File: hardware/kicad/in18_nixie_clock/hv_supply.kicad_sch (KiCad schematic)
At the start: 2 parts

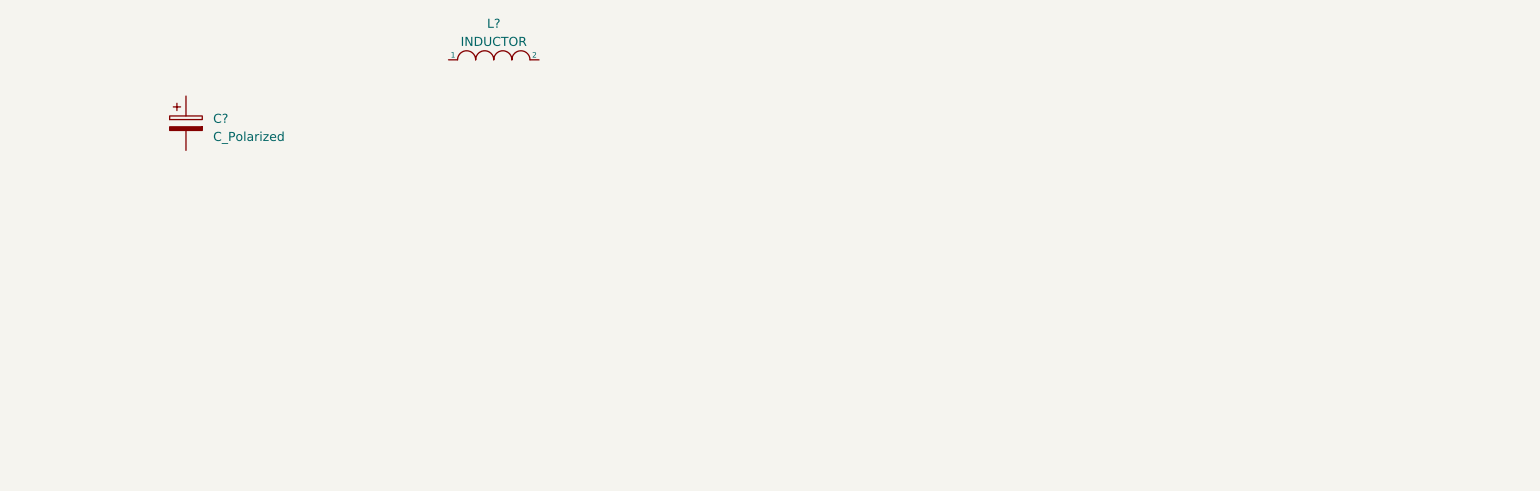
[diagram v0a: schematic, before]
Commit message: Delete backups. Add HV supply schematic
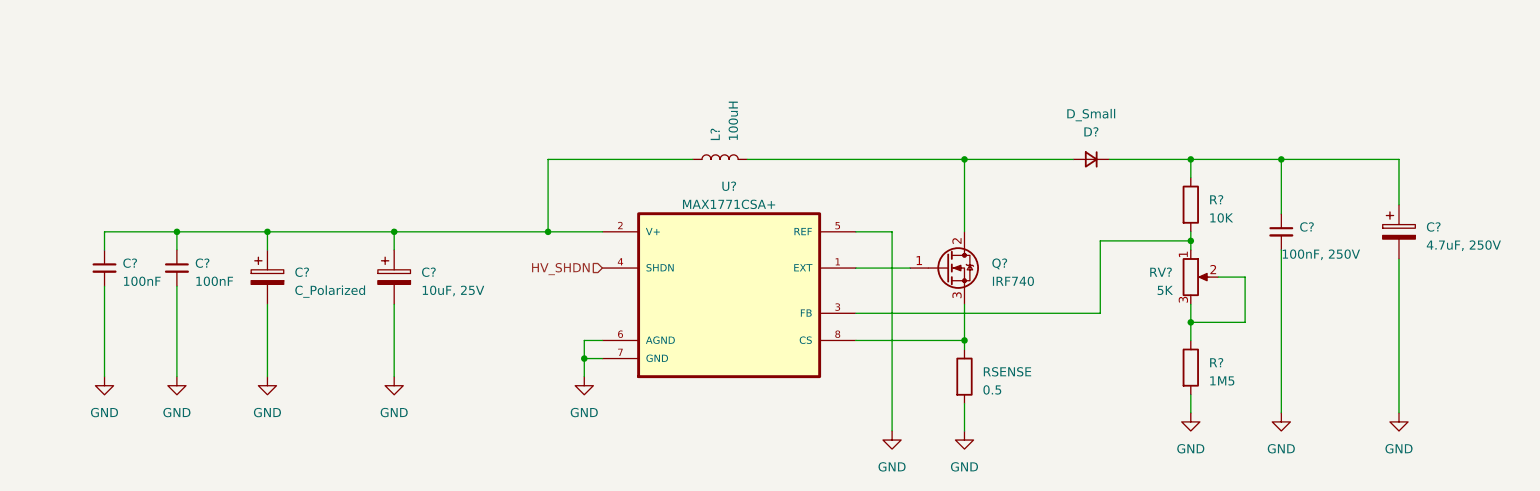
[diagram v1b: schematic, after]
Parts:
- removed L?: INDUCTOR, symbol pspice:INDUCTOR
- added C?: 4.7uF, 250V, symbol Device:C_Polarized
- added C?: 10uF, 25V, symbol Device:C_Polarized
- added C? (x2): 100nF, Capacitor_SMD:C_0805_2012Metric_Pad1.18x1.45mm_HandSolder, symbol Device:C_Small
- added C?: 100nF, 250V, Capacitor_SMD:C_0805_2012Metric_Pad1.18x1.45mm_HandSolder, symbol Device:C_Small
- added D?: D_Small, symbol Device:D_Small
- added L?: 100uH, symbol Device:L
- added Q?: IRF740, Package_TO_SOT_THT:TO-220-3_Vertical, symbol Transistor_FET:IRF740
- added R?: 1M5, symbol Device:R
- added R?: 10K, symbol Device:R
- added RSENSE: 0.5, symbol Device:R
- added RV?: 5K, symbol Device:R_Potentiometer
- added U?: MAX1771CSA+, SOIC127P600X175-8N, symbol MAX1771CSA:MAX1771CSA+
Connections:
- net at C?.1: now also C?.1, C?.1, C?.1, L?.1, U?.2 (V+)
- net GND: now reaches C?.2
- net GND: now also C?.2, C?.2, C?.2, C?.2, C?.2, R?.2, RSENSE.2, U?.5 (REF), U?.6 (AGND), U?.7 (GND)
- new net: R?.2, RV?.1, U?.3 (FB)
- new net: R?.1, RV?.2, RV?.3
- new net: Q?.1 (G), U?.1 (EXT)
- new net: D?.2 (A), L?.2, Q?.2 (D)
- new net: Q?.3 (S), RSENSE.1, U?.8 (CS)
- new net: C?.1, C?.1, D?.1 (K), R?.1
- new net HV_SHDN: U?.4 (SHDN)
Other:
- moved on the sheet: C?

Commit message: Add several schematics
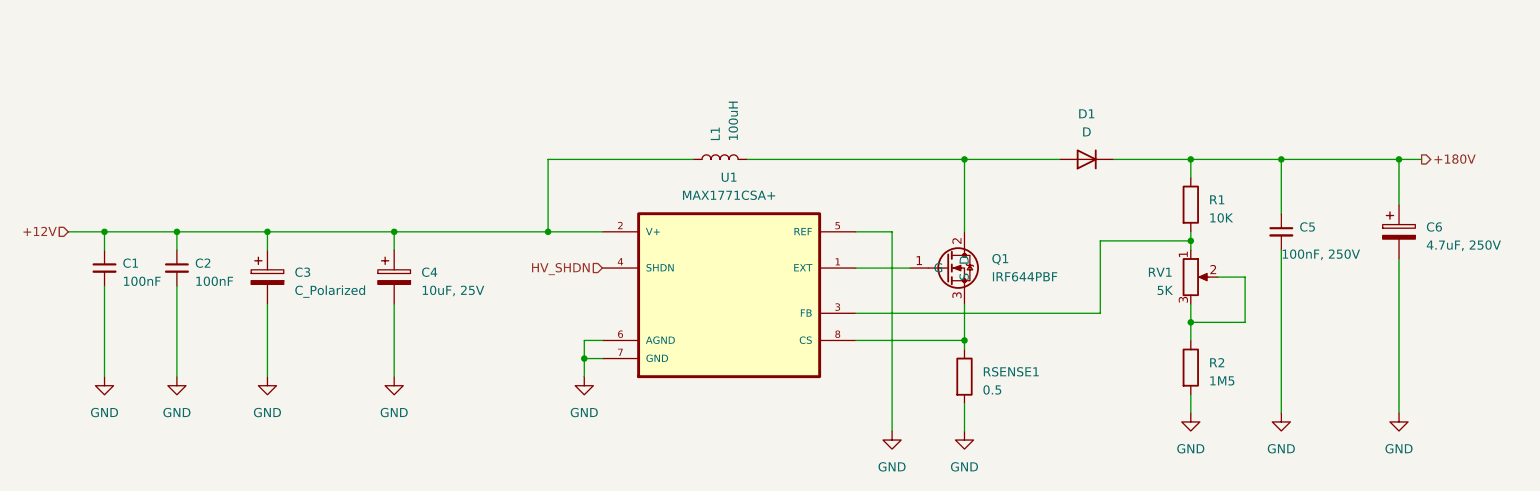
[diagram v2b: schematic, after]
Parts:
- removed D?: D_Small, symbol Device:D_Small
- removed Q?: IRF740, Package_TO_SOT_THT:TO-220-3_Vertical, symbol Transistor_FET:IRF740
- removed U?: MAX1771CSA+, SOIC127P600X175-8N, symbol MAX1771CSA:MAX1771CSA+
- added D1: D, symbol Device:D
- added Q1: IRF644PBF, TO254P465X1024X2050-3P, symbol FET_user:IRF644PBF
- added U1: MAX1771CSA+, Regulator_user:SOIC127P600X175-8N, symbol Regulator_user:MAX1771CSA+
- gave numbers to parts that had none: 10
- renumbered RSENSE to RSENSE1
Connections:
- net GND: now also U1.5 (REF), U1.6 (AGND), U1.7 (GND)
- net HV_SHDN: now also U1.4 (SHDN)
- net at R1.2, RV1.1: now also U1.3 (FB)
- net at L1.2: now also D1.2 (A), Q1.2 (D)
- net at RSENSE1.1: now also Q1.3 (S), U1.8 (CS)
- net +180V: now reaches C5.1, C6.1, R1.1
- net +180V: now also D1.1 (K)
- net +12V: now reaches C1.1, C2.1, C3.1, C4.1, L1.1
- net +12V: now also U1.2 (V+)
- new net: Q1.1 (G), U1.1 (EXT)
